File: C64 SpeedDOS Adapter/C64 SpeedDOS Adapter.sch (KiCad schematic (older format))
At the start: 6 parts, among them J1 C64_User_Port, J2 SpeedDOS, M1 Mounting, M2 Mounting, M3 Mounting, M4 Mounting

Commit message: Updated gerber files and small tweaks
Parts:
- added JP1: CA2, solder_bridge:bridge, symbol Jumper:SolderJumper_2_Bridged
- added JP2: CB1, solder_bridge:bridge_r, symbol Jumper:SolderJumper_2_Bridged
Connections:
- net VIA_CA2: now also JP1.1 (A); no longer J2.1 (Pin_1)
- net VIA_CB1: now also JP2.1 (A); no longer J2.10 (Pin_10)
- new net: J2.1 (Pin_1), JP1.2 (B)
- new net: J2.10 (Pin_10), JP2.2 (B)
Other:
- moved on the sheet: J2
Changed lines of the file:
@@
 L speed_dos:Speed_DOS_IDC J2
 U 1 1 5EF167B3
-P 7975 2700
-F 0 "J2" H 7975 3125 50  0000 C CNN
-F 1 "SpeedDOS" H 7975 3025 50  0000 C CNN
-F 2 "speed_dos:SpeedDOS_IDC" H 7975 2700 50  0001 C CNN
-F 3 "~" H 7975 2700 50  0001 C CNN
-	1    7975 2700
+P 8200 2700
+F 0 "J2" H 8200 3125 50  0000 C CNN
+F 1 "SpeedDOS" H 8200 3025 50  0000 C CNN
+F 2 "speed_dos:SpeedDOS_IDC" H 8200 2700 50  0001 C CNN
+F 3 "~" H 8200 2700 50  0001 C CNN
+	1    8200 2700
 	1    0    0    -1
 $EndComp
@@
 L power:GND #PWR01
 U 1 1 5EF2A7F5
-P 8525 3475
-F 0 "#PWR01" H 8525 3225 50  0001 C CNN
-F 1 "GND" H 8530 3302 50  0000 C CNN
-F 2 "" H 8525 3475 50  0001 C CNN
-F 3 "" H 8525 3475 50  0001 C CNN
-	1    8525 3475
-	1    0    0    -1
-$EndComp
-Wire Wire Line
-	8450 3400 8525 3400
-Wire Wire Line
-	8525 3400 8525 3475
+P 8750 3475
+F 0 "#PWR01" H 8750 3225 50  0001 C CNN
+F 1 "GND" H 8755 3302 50  0000 C CNN
+F 2 "" H 8750 3475 50  0001 C CNN
+F 3 "" H 8750 3475 50  0001 C CNN
+	1    8750 3475
+	1    0    0    -1
+$EndComp
+Wire Wire Line
+	8675 3400 8750 3400
+Wire Wire Line
+	8750 3400 8750 3475
 Text Label 7025 2600 0    50   ~ 0
 VIA_PA0
@@
 VIA_CB1
 Wire Wire Line
-	7000 2500 7525 2500
-Wire Wire Line
-	7525 2600 7000 2600
-Wire Wire Line
-	7000 2700 7525 2700
-Wire Wire Line
-	7000 2800 7525 2800
-Wire Wire Line
-	7525 2900 7000 2900
-Wire Wire Line
-	7000 3000 7525 3000
-Wire Wire Line
-	7000 3100 7525 3100
-Wire Wire Line
-	7525 3200 7000 3200
-Wire Wire Line
-	7000 3300 7525 3300
-Wire Wire Line
-	7000 3400 7525 3400
+	7000 2500 7450 2500
 $Comp
 L C64-User-Port:C64_User_Port J1
@@
 	1    0    0    -1
 $EndComp
+$Comp
+L Jumper:SolderJumper_2_Bridged JP1
+U 1 1 60764DE4
+P 7600 2500
+F 0 "JP1" H 7600 2675 50  0000 C CNN
+F 1 "CA2" H 7600 2600 50  0000 C CNN
+F 2 "solder_bridge:bridge" H 7600 2500 50  0001 C CNN
+F 3 "~" H 7600 2500 50  0001 C CNN
+	1    7600 2500
+	1    0    0    -1
+$EndComp
+$Comp
+L Jumper:SolderJumper_2_Bridged JP2
+U 1 1 6077FA79
+P 7600 3400
+F 0 "JP2" H 7600 3300 50  0000 C CNN
+F 1 "CB1" H 7600 3225 50  0000 C CNN
+F 2 "solder_bridge:bridge_r" H 7600 3400 50  0001 C CNN
+F 3 "~" H 7600 3400 50  0001 C CNN
+	1    7600 3400
+	1    0    0    -1
+$EndComp
+Wire Wire Line
+	7000 2600 7750 2600
+Wire Wire Line
+	7000 2700 7750 2700
+Wire Wire Line
+	7000 2800 7750 2800
+Wire Wire Line
+	7000 2900 7750 2900
+Wire Wire Line
+	7000 3000 7750 3000
+Wire Wire Line
+	7000 3100 7750 3100
+Wire Wire Line
+	7000 3200 7750 3200
+Wire Wire Line
+	7000 3300 7750 3300
+Wire Wire Line
+	7450 3400 7000 3400
+Wire Bus Line
+	6900 1800 6900 3300
 Wire Bus Line
 	3850 1800 3850 3300
-Wire Bus Line
-	6900 1800 6900 3300
 $EndSCHEMATC

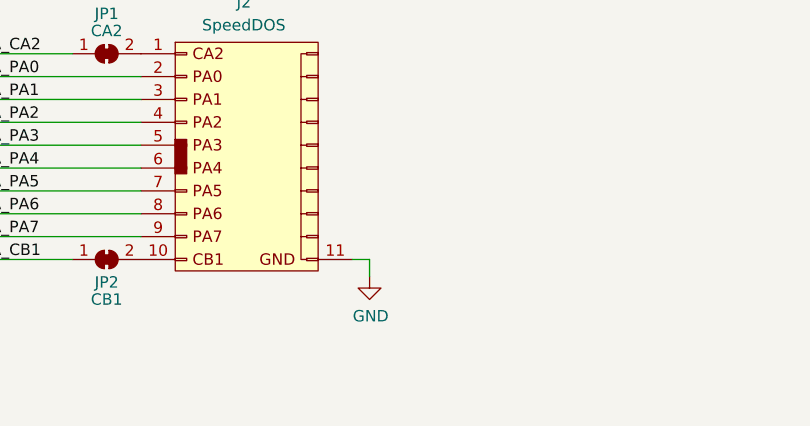
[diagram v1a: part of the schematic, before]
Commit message: Added GND jumper to adapter
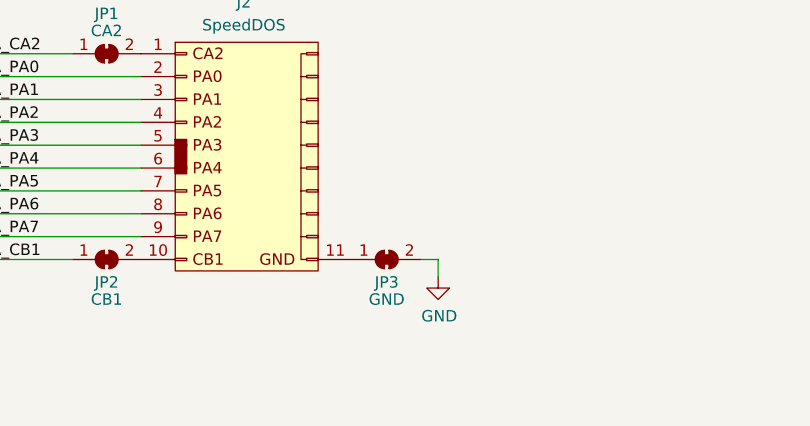
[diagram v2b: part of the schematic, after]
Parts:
- added JP3: GND, solder_bridge:bridge, symbol Jumper:SolderJumper_2_Bridged
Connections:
- net GND: now also JP3.2 (B); no longer J2.11 (Pin_11)
- new net: J2.11 (Pin_11), JP3.1 (A)
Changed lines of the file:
@@
 L power:GND #PWR01
 U 1 1 5EF2A7F5
-P 8750 3475
-F 0 "#PWR01" H 8750 3225 50  0001 C CNN
-F 1 "GND" H 8755 3302 50  0000 C CNN
-F 2 "" H 8750 3475 50  0001 C CNN
-F 3 "" H 8750 3475 50  0001 C CNN
-	1    8750 3475
-	1    0    0    -1
-$EndComp
-Wire Wire Line
-	8675 3400 8750 3400
-Wire Wire Line
-	8750 3400 8750 3475
+P 9050 3475
+F 0 "#PWR01" H 9050 3225 50  0001 C CNN
+F 1 "GND" H 9055 3302 50  0000 C CNN
+F 2 "" H 9050 3475 50  0001 C CNN
+F 3 "" H 9050 3475 50  0001 C CNN
+	1    9050 3475
+	1    0    0    -1
+$EndComp
+Wire Wire Line
+	8975 3400 9050 3400
+Wire Wire Line
+	9050 3400 9050 3475
 Text Label 7025 2600 0    50   ~ 0
 VIA_PA0
@@
 Wire Wire Line
 	7450 3400 7000 3400
+$Comp
+L Jumper:SolderJumper_2_Bridged JP3
+U 1 1 608B4F78
+P 8825 3400
+F 0 "JP3" H 8825 3300 50  0000 C CNN
+F 1 "GND" H 8825 3225 50  0000 C CNN
+F 2 "solder_bridge:bridge" H 8825 3400 50  0001 C CNN
+F 3 "~" H 8825 3400 50  0001 C CNN
+	1    8825 3400
+	1    0    0    -1
+$EndComp
 Wire Bus Line
 	6900 1800 6900 3300
